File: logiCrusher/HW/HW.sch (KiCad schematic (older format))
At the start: 11 parts, among them J1 Left, J3 Conn_02x05_Odd_Even, J4 Right, U3 R-783.3-0.5

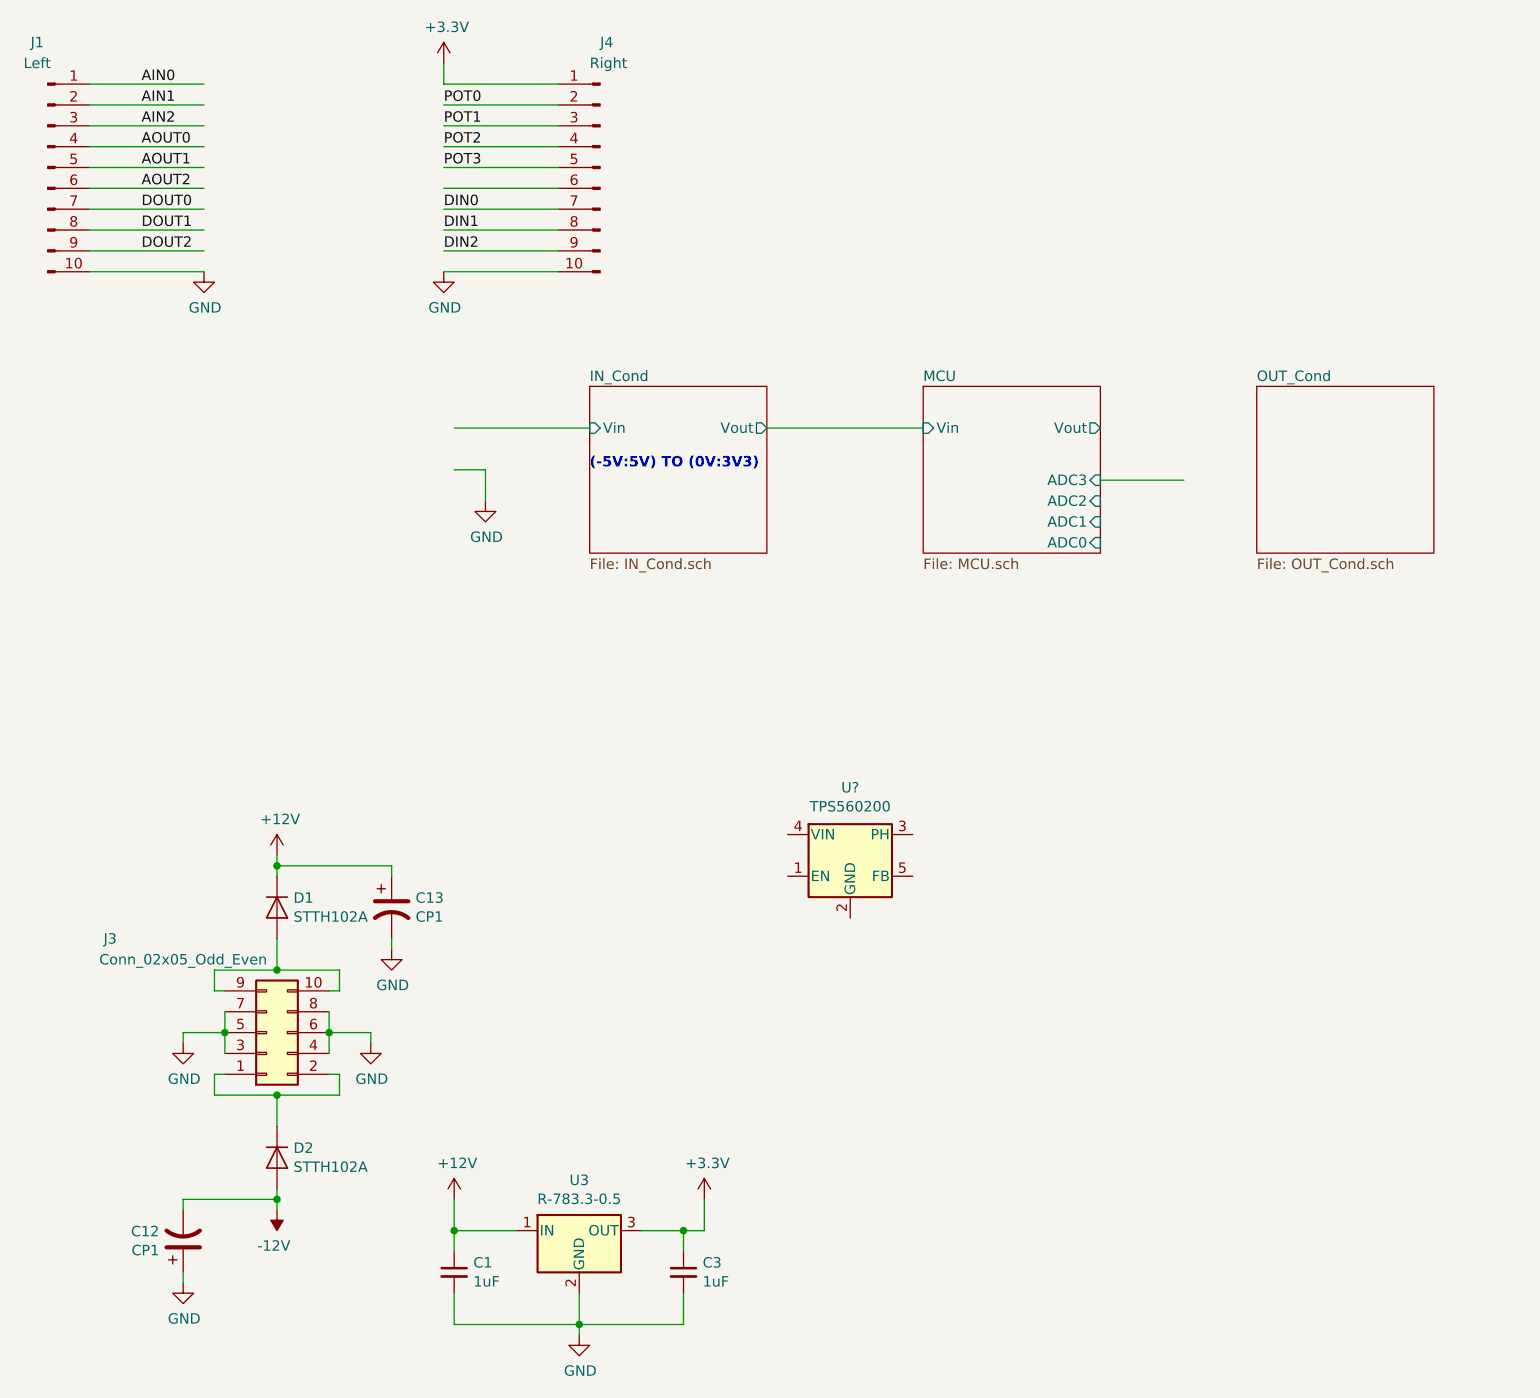
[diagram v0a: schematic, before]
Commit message: Worked on the layout for the logicrusher
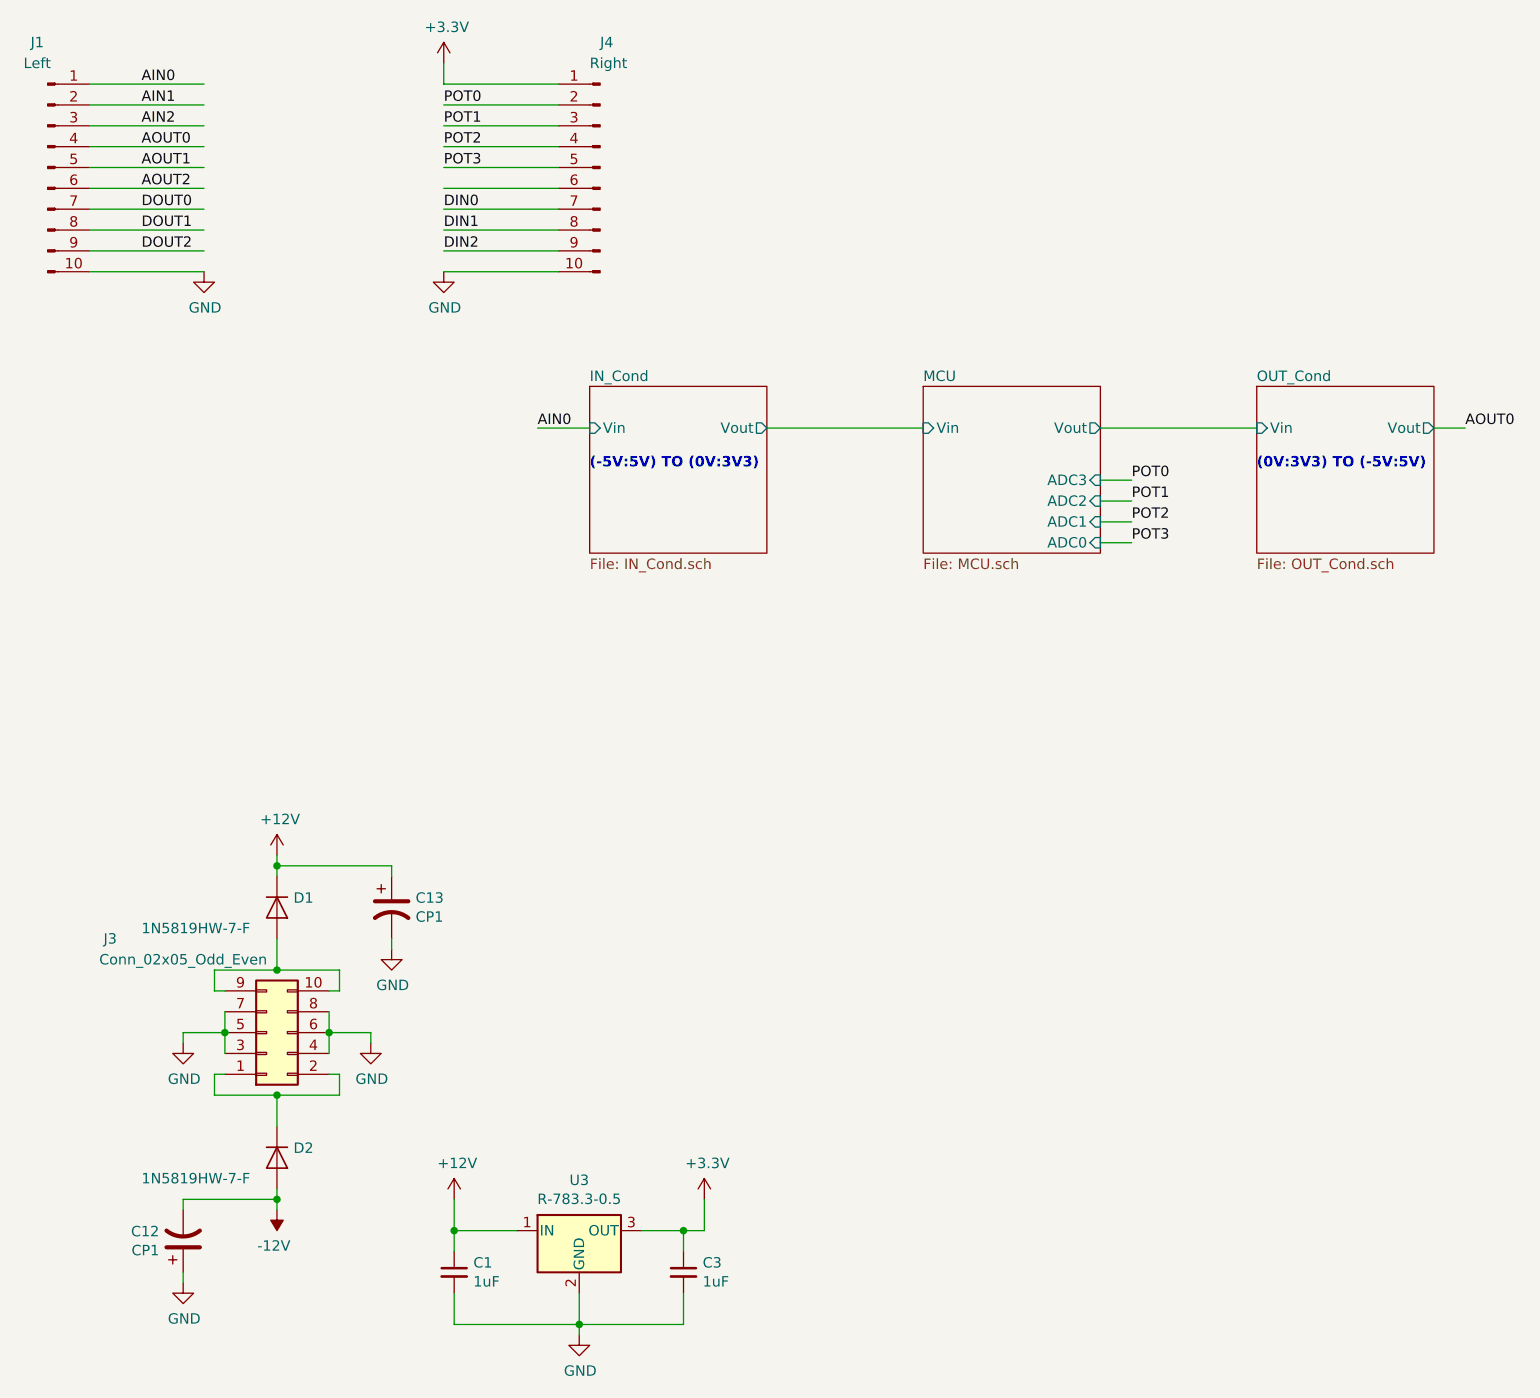
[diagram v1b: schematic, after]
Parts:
- removed U?: TPS560200, Package_TO_SOT_SMD:SOT-23-5, symbol Regulator_Switching:TPS560200
- D1, D2: value STTH102A -> 1N5819HW-7-F; footprint Diode_SMD:D_SMA -> Diode_SMD:D_SOD-123
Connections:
- wire segments 71 -> 74
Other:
- note added: "(0V:3V3) TO (-5V:5V)"
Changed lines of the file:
@@
 P 2100 5100
 F 0 "D1" V 2054 5179 50  0000 L CNN
-F 1 "STTH102A" V 2145 5179 50  0000 L CNN
-F 2 "Diode_SMD:D_SMA" H 2100 4925 50  0001 C CNN
-F 3 "http://www.vishay.com/docs/88503/1n4001.pdf" H 2100 5100 50  0001 C CNN
+F 1 "1N5819HW-7-F" V 2200 4450 50  0000 L CNN
+F 2 "Diode_SMD:D_SOD-123" H 2100 4925 50  0001 C CNN
+F 3 "" H 2100 5100 50  0001 C CNN
 	1    2100 5100
 	0    1    1    0
@@
 P 2100 6300
 F 0 "D2" V 2054 6379 50  0000 L CNN
-F 1 "STTH102A" V 2145 6379 50  0000 L CNN
-F 2 "Diode_SMD:D_SMA" H 2100 6125 50  0001 C CNN
+F 1 "1N5819HW-7-F" V 2200 5650 50  0000 L CNN
+F 2 "Diode_SMD:D_SOD-123" H 2100 6125 50  0001 C CNN
 F 3 "http://www.vishay.com/docs/88503/1n4001.pdf" H 2100 6300 50  0001 C CNN
 	1    2100 6300
@@
 F0 "OUT_Cond" 50
 F1 "OUT_Cond.sch" 50
+F2 "Vout" O R 7650 2800 50
+F3 "Vin" I L 6800 2800 50
 $EndSheet
 Wire Wire Line
-	2950 2800 3600 2800
-Wire Wire Line
-	2950 3000 3100 3000
-Wire Wire Line
-	3100 3000 3100 3150
-$Comp
-L power:GND #PWR08
-U 1 1 5CB57BF9
-P 3100 3150
-F 0 "#PWR08" H 3100 2900 50  0001 C CNN
-F 1 "GND" H 3105 2977 50  0000 C CNN
-F 2 "" H 3100 3150 50  0001 C CNN
-F 3 "" H 3100 3150 50  0001 C CNN
-	1    3100 3150
-	1    0    0    -1
-$EndComp
+	3350 2800 3600 2800
 Text Notes 3600 3000 0    50   ~ 10
 (-5V:5V) TO (0V:3V3)
-Wire Wire Line
-	6050 3050 6450 3050
 Wire Wire Line
 	4450 2800 5200 2800
@@
 Text Label 2900 1950 0    50   ~ 0
 DIN2
-$Comp
-L Regulator_Switching:TPS560200 U?
-U 1 1 5CBCC094
-P 4850 4850
-F 0 "U?" H 4850 5175 50  0000 C CNN
-F 1 "TPS560200" H 4850 5084 50  0000 C CNN
-F 2 "Package_TO_SOT_SMD:SOT-23-5" H 4900 4600 50  0001 L CNN
-F 3 "http://www.ti.com/lit/ds/symlink/tps560200.pdf" H 4600 4500 50  0001 C CNN
-	1    4850 4850
-	1    0    0    -1
-$EndComp
+Text Label 3350 2800 0    50   ~ 0
+AIN0
+Wire Wire Line
+	6050 2800 6800 2800
+Text Label 7800 2800 0    50   ~ 0
+AOUT0
+Wire Wire Line
+	7800 2800 7650 2800
+Text Notes 6800 3000 0    50   ~ 10
+(0V:3V3) TO (-5V:5V)
+Text Label 6200 3050 0    50   ~ 0
+POT0
+Text Label 6200 3150 0    50   ~ 0
+POT1
+Text Label 6200 3250 0    50   ~ 0
+POT2
+Text Label 6200 3350 0    50   ~ 0
+POT3
+Wire Wire Line
+	6050 3050 6200 3050
+Wire Wire Line
+	6200 3150 6050 3150
+Wire Wire Line
+	6050 3250 6200 3250
+Wire Wire Line
+	6200 3350 6050 3350
 $EndSCHEMATC

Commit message: Spend a lot of time working on the logicCrusher HW
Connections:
- net labels added: D0, D1, D2, D3, D4, D5
- net labels removed: DIN0, DIN1, DIN2, DOUT0, DOUT1, DOUT2
- wire segments 74 -> 80
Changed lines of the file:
@@
 $EndComp
 $Sheet
-S 5200 2600 850  800
+S 5200 2600 850  1100
 U 5CB08311
 F0 "MCU" 50
@@
 F6 "ADC2" I R 6050 3150 50
 F7 "ADC3" I R 6050 3050 50
+F8 "D0" O L 5200 3050 50
+F9 "D1" O L 5200 3150 50
+F10 "D2" O L 5200 3250 50
+F11 "D3" O L 5200 3350 50
+F12 "D4" I L 5200 3450 50
+F13 "D5" I L 5200 3550 50
 $EndSheet
 $Sheet
@@
 POT3
 Text Label 1450 1750 0    50   ~ 0
-DOUT0
+D0
 Text Label 1450 1850 0    50   ~ 0
-DOUT1
+D1
 Text Label 1450 1950 0    50   ~ 0
-DOUT2
+D2
 Text Label 2900 1750 0    50   ~ 0
-DIN0
+D3
 Text Label 2900 1850 0    50   ~ 0
-DIN1
+D4
 Text Label 2900 1950 0    50   ~ 0
-DIN2
+D5
 Text Label 3350 2800 0    50   ~ 0
 AIN0
@@
 Wire Wire Line
 	6200 3350 6050 3350
+Wire Wire Line
+	5200 3050 4950 3050
+Wire Wire Line
+	5200 3150 4950 3150
+Wire Wire Line
+	5200 3250 4950 3250
+Wire Wire Line
+	5200 3350 4950 3350
+Wire Wire Line
+	5200 3450 4950 3450
+Wire Wire Line
+	5200 3550 4950 3550
+Text Label 4950 3050 0    50   ~ 0
+D0
+Text Label 4950 3150 0    50   ~ 0
+D1
+Text Label 4950 3250 0    50   ~ 0
+D2
+Text Label 4950 3350 0    50   ~ 0
+D3
+Text Label 4950 3450 0    50   ~ 0
+D4
+Text Label 4950 3550 0    50   ~ 0
+D5
 $EndSCHEMATC
